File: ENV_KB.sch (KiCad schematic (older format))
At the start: 178 parts, among them J1 USB_B_Micro

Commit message: general housekeeping.
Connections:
- net USBVBUS: now reaches J1.1 (VBUS)
- net USBVBUS: now also RPI1.40 (VBUS)
- net USBDM: now reaches J1.2 (D-)
- net USBDM: now also RPI1.TP2 (USB_DM)
- net USBDP: now reaches J1.3 (D+)
- net USBDP: now also RPI1.TP3 (USB_DP)
- net USBGND: now reaches J1.5 (GND)
- net USBGND: now also RPI1.TP1 (GND_L)
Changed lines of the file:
@@
 Text GLabel 13750 10900 2    50   Input ~ 0
 col16
+Text GLabel 12800 8900 1    50   Input ~ 0
+USBGND
+Text GLabel 10800 9300 2    50   Input ~ 0
+USBGND
+Text GLabel 12950 8900 1    50   Input ~ 0
+USBDM
+Text GLabel 10500 9000 1    50   Input ~ 0
+USBDM
+Text GLabel 10400 9000 1    50   Input ~ 0
+USBDP
+Text GLabel 13100 8900 1    50   Input ~ 0
+USBDP
+Text GLabel 13650 9100 2    50   Input ~ 0
+USBVBUS
+Text GLabel 10200 9000 1    50   Input ~ 0
+USBVBUS
 $EndSCHEMATC

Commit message: This should be Ready.
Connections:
- net row0: now also RPI1.26 (GPIO20); no longer RPI1.34 (GPIO28_ADC2)
- net row2: now also RPI1.27 (GPIO21); no longer RPI1.32 (GPIO27_ADC1)
- net row3: now also RPI1.29 (GPIO22); no longer RPI1.31 (GPIO26_ADC0)
- net row4: now also RPI1.31 (GPIO26_ADC0); no longer RPI1.29 (GPIO22)
- net row5: now also RPI1.32 (GPIO27_ADC1); no longer RPI1.27 (GPIO21)
- net row6: now also RPI1.34 (GPIO28_ADC2); no longer RPI1.26 (GPIO20)
- net USBDM renamed USB2_N
- net USBDP renamed USB2_P
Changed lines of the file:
@@
 	0    -1   -1   0
 $EndComp
-Text GLabel 13750 10500 2    50   Input ~ 0
+Text GLabel 13750 9700 2    50   Input ~ 0
 row6
+Text GLabel 13750 9900 2    50   Input ~ 0
+row5
 Text GLabel 13750 10400 2    50   Input ~ 0
-row5
-Text GLabel 13750 9900 2    50   Input ~ 0
 row2
+Text GLabel 13750 10200 2    50   Input ~ 0
+row3
 Text GLabel 13750 10000 2    50   Input ~ 0
-row3
-Text GLabel 13750 10200 2    50   Input ~ 0
 row4
 Text GLabel 13750 10600 2    50   Input ~ 0
@@
 Text GLabel 13750 10700 2    50   Input ~ 0
 col15
-Text GLabel 13750 9700 2    50   Input ~ 0
+Text GLabel 13750 10500 2    50   Input ~ 0
 row0
 Wire Wire Line
@@
 USBGND
 Text GLabel 12950 8900 1    50   Input ~ 0
-USBDM
+USB2_N
 Text GLabel 10500 9000 1    50   Input ~ 0
-USBDM
+USB2_N
 Text GLabel 10400 9000 1    50   Input ~ 0
-USBDP
+USB2_P
 Text GLabel 13100 8900 1    50   Input ~ 0
-USBDP
+USB2_P
 Text GLabel 13650 9100 2    50   Input ~ 0
 USBVBUS

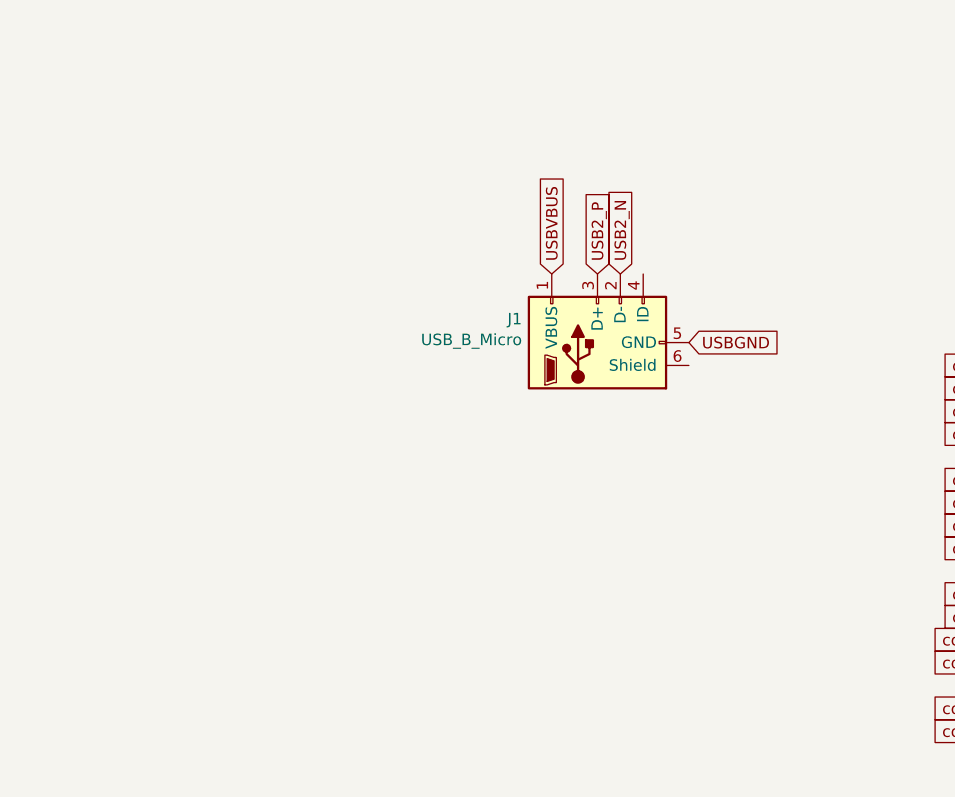
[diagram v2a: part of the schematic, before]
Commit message: replaced Micro B with Type C due to parts avaliability
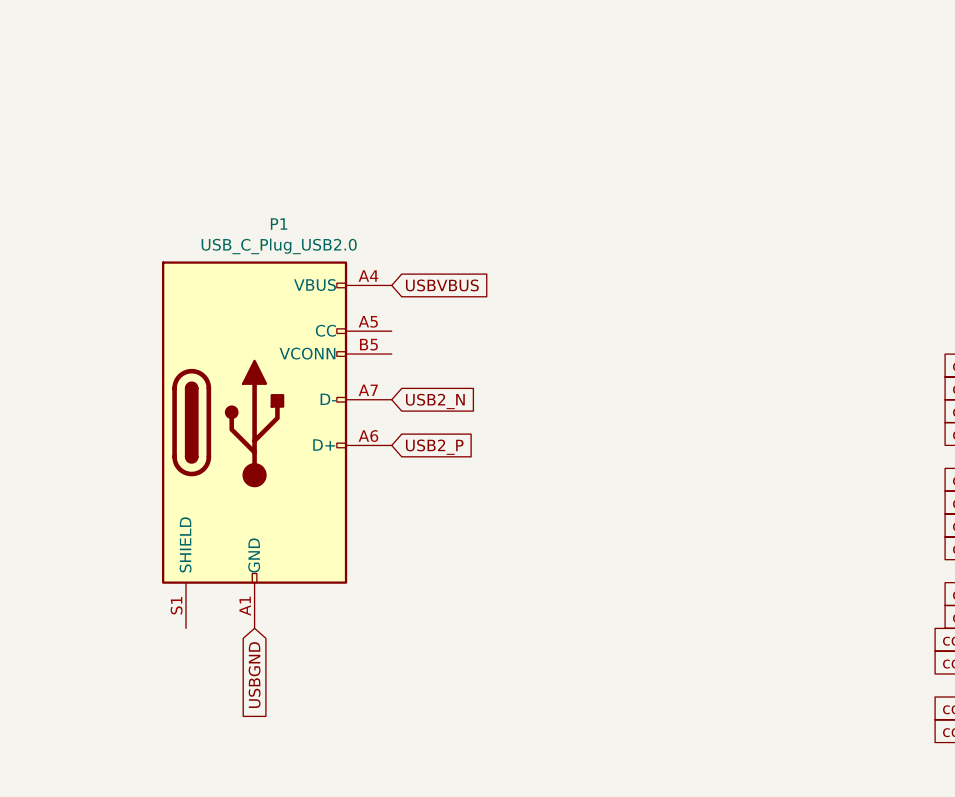
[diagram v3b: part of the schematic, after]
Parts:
- removed J1: USB_B_Micro, Connector_USB:USB_Micro-B_Wuerth_629105150521, symbol Connector:USB_B_Micro
- added P1: USB_C_Plug_USB2.0, Connector_USB:USB_C_Receptacle_HRO_TYPE-C-31-M-12, symbol Connector:USB_C_Plug_USB2.0
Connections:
- net USB2_N: now also P1.A7 (D-)
- net USB2_P: now also P1.A6 (D+)
- net USBGND: now also P1.A1 (GND), P1.A12 (GND), P1.B1 (GND), P1.B12 (GND)
- net USBVBUS: now also P1.A4 (VBUS), P1.A9 (VBUS), P1.B4 (VBUS), P1.B9 (VBUS)
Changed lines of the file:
@@
 	1    0    0    -1
-$EndComp
-$Comp
-L Connector:USB_B_Micro J1
-U 1 1 6031CA0E
-P 10400 9300
-F 0 "J1" V 10503 9630 50  0000 L CNN
-F 1 "USB_B_Micro" V 10412 9630 50  0000 L CNN
-F 2 "Connector_USB:USB_Micro-B_Wuerth_629105150521" H 10550 9250 50  0001 C CNN
-F 3 "~" H 10550 9250 50  0001 C CNN
-	1    10400 9300
-	0    -1   -1   0
 $EndComp
 Wire Wire Line
@@
 Text GLabel 12800 8900 1    50   Input ~ 0
 USBGND
-Text GLabel 10800 9300 2    50   Input ~ 0
-USBGND
 Text GLabel 12950 8900 1    50   Input ~ 0
 USB2_N
-Text GLabel 10500 9000 1    50   Input ~ 0
+Text GLabel 9500 9550 2    50   Input ~ 0
 USB2_N
-Text GLabel 10400 9000 1    50   Input ~ 0
+Text GLabel 9500 9750 2    50   Input ~ 0
 USB2_P
 Text GLabel 13100 8900 1    50   Input ~ 0
@@
 Text GLabel 13650 9100 2    50   Input ~ 0
 USBVBUS
-Text GLabel 10200 9000 1    50   Input ~ 0
+Text GLabel 8900 10550 3    50   Input ~ 0
+USBGND
+Text GLabel 9500 9050 2    50   Input ~ 0
 USBVBUS
+$Comp
+L Connector:USB_C_Plug_USB2.0 P1
+U 1 1 6035DC13
+P 8900 9650
+F 0 "P1" H 9007 10517 50  0000 C CNN
+F 1 "USB_C_Plug_USB2.0" H 9007 10426 50  0000 C CNN
+F 2 "Connector_USB:USB_C_Receptacle_HRO_TYPE-C-31-M-12" H 9050 9650 50  0001 C CNN
+F 3 "https://www.usb.org/sites/default/files/documents/usb_type-c.zip" H 9050 9650 50  0001 C CNN
+	1    8900 9650
+	1    0    0    -1
+$EndComp
 $EndSCHEMATC

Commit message: some random changes
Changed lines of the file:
@@
 	1350 3400 2350 3400
 Wire Wire Line
-	-50  2400 1450 2400
+	900  2400 2400 2400
 Wire Wire Line
 	1350 1400 3350 1400
@@
 $Comp
 L MX_Alps_Hybrid:MX-NoLED K_0
-U 1 1 00000001
+U 1 1 603522C8
 P 1400 1000
 F 0 "K_0" H 1400 1233 60  0000 C CNN
@@
 $Comp
 L MX_Alps_Hybrid:MX-NoLED K_1
-U 1 1 00000011
+U 1 1 603522CA
 P 3400 1000
 F 0 "K_1" H 3400 1233 60  0000 C CNN
@@
 $Comp
 L MX_Alps_Hybrid:MX-NoLED K_3
-U 1 1 00000031
+U 1 1 603522CE
 P 5400 1000
 F 0 "K_3" H 5400 1233 60  0000 C CNN
@@
 $Comp
 L MX_Alps_Hybrid:MX-NoLED K_4
-U 1 1 00000041
+U 1 1 603522D0
 P 6400 1000
 F 0 "K_4" H 6400 1233 60  0000 C CNN
@@
 $Comp
 L MX_Alps_Hybrid:MX-NoLED K_5
-U 1 1 00000051
+U 1 1 603522D2
 P 8400 1000
 F 0 "K_5" H 8400 1233 60  0000 C CNN
@@
 $Comp
 L MX_Alps_Hybrid:MX-NoLED K_7
-U 1 1 00000071
+U 1 1 603522D6
 P 10400 1000
 F 0 "K_7" H 10400 1233 60  0000 C CNN
@@
 $Comp
 L Device:D_Small D7
-U 1 1 00000070
+U 1 1 603522D5
 P 10350 1300
 F 0 "D7" V 10420 1200 50  0000 R CNN
@@
 $Comp
 L Device:D_Small D8
-U 1 1 00000080
+U 1 1 603522D7
 P 11350 1300
 F 0 "D8" V 11420 1200 50  0000 R CNN
@@
 $Comp
 L MX_Alps_Hybrid:MX-NoLED K_9
-U 1 1 00000091
+U 1 1 603522DA
 P 12400 1000
 F 0 "K_9" H 12400 1233 60  0000 C CNN
@@
 $Comp
 L Device:D_Small D9
-U 1 1 00000090
+U 1 1 603522D9
 P 12350 1300
 F 0 "D9" V 12420 1200 50  0000 R CNN
@@
 $Comp
 L MX_Alps_Hybrid:MX-NoLED K_10
-U 1 1 00000101
+U 1 1 603522DC
 P 13400 1000
 F 0 "K_10" H 13400 1233 60  0000 C CNN
@@
 $Comp
 L Device:D_Small D6
-U 1 1 00000060
+U 1 1 603522D3
 P 9350 1300
 F 0 "D6" V 9420 1200 50  0000 R CNN
@@
 $Comp
 L Device:D_Small D5
-U 1 1 00000050
+U 1 1 603522D1
 P 8350 1300
 F 0 "D5" V 8420 1200 50  0000 R CNN
@@
 $Comp
 L Device:D_Small D4
-U 1 1 00000040
+U 1 1 603522CF
 P 6350 1300
 F 0 "D4" V 6420 1200 50  0000 R CNN
@@
 $Comp
 L Device:D_Small D3
-U 1 1 00000030
+U 1 1 603522CD
 P 5350 1300
 F 0 "D3" V 5420 1200 50  0000 R CNN
@@
 $Comp
 L Device:D_Small D2
-U 1 1 00000020
+U 1 1 603522CB
 P 4350 1300
 F 0 "D2" V 4420 1200 50  0000 R CNN

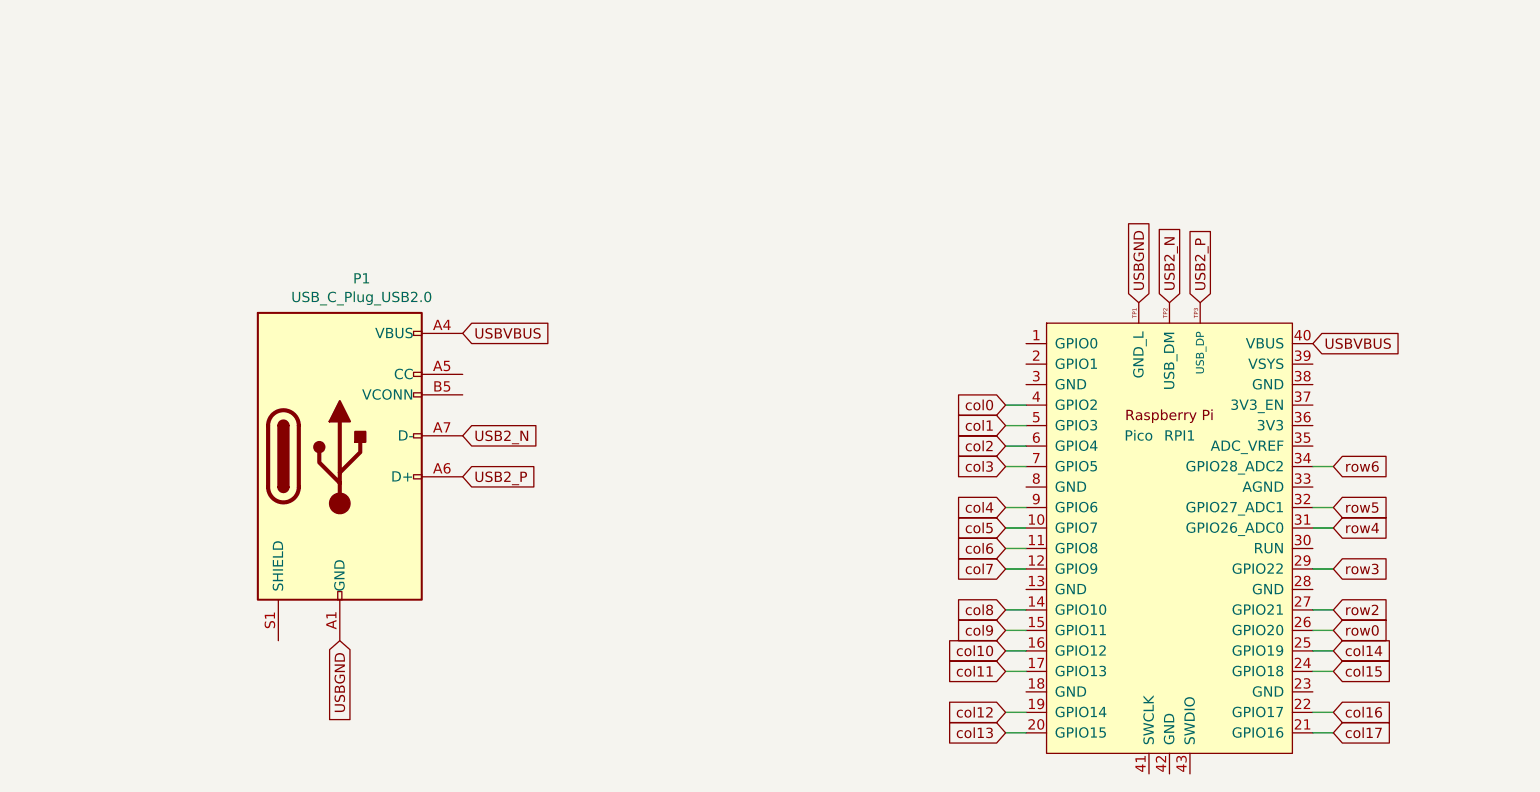
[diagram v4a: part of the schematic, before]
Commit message: Adjusted things + typeC CC pins
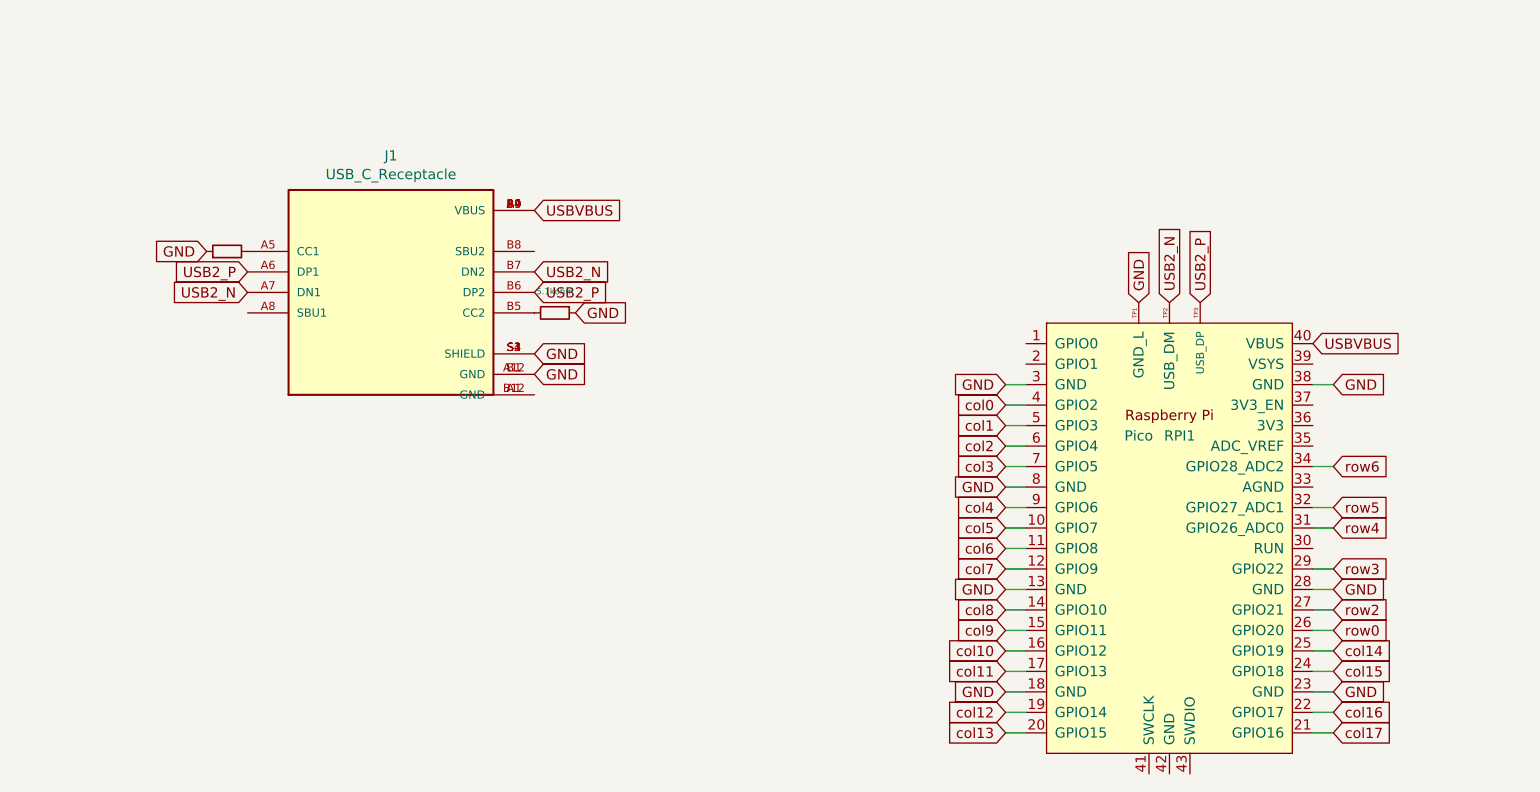
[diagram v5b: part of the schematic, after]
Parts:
- removed P1: USB_C_Plug_USB2.0, Connector_USB:USB_C_Receptacle_HRO_TYPE-C-31-M-12, symbol Connector:USB_C_Plug_USB2.0
- added J1: USB_C_Receptacle, Type-C-Bits:HRO_TYPE-C-31-M-12, symbol Type-C-Lib:TYPE-C-31-M-12
- added RESISTOR1, RESISTOR2: 5.1kohm, Resistor_SMD:R_0402_1005Metric, symbol Device:R_Small
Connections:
- net USBGND is gone; now on net GND: RPI1.TP1 (GND_L)
- net USB2_N: now also J1.A7 (DN1), J1.B7 (DN2)
- net USB2_P: now also J1.A6 (DP1), J1.B6 (DP2)
- net USBVBUS: now also J1.A4 (VBUS), J1.A9 (VBUS), J1.B4 (VBUS), J1.B9 (VBUS)
- net GND: now reaches RPI1.13 (GND)
- net GND: now also RPI1.18 (GND), RPI1.23 (GND), RPI1.28 (GND), RPI1.3 (GND), RPI1.38 (GND), RPI1.8 (GND), J1.A12 (GND), J1.B1 (GND), J1.S1 (SHIELD), J1.S2 (SHIELD), J1.S3 (SHIELD), J1.S4 (SHIELD), RESISTOR1.1, RESISTOR2.1
- new net: J1.B5 (CC2), RESISTOR1.2
- new net: J1.A5 (CC1), RESISTOR2.2
- new net: J1.A1 (GND), J1.B12 (GND)
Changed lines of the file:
@@
 col16
 Text GLabel 12800 8900 1    50   Input ~ 0
-USBGND
+GND
 Text GLabel 12950 8900 1    50   Input ~ 0
 USB2_N
-Text GLabel 9500 9550 2    50   Input ~ 0
+Text GLabel 8450 8850 0    50   Input ~ 0
 USB2_N
-Text GLabel 9500 9750 2    50   Input ~ 0
+Text GLabel 9850 8850 2    50   Input ~ 0
 USB2_P
 Text GLabel 13100 8900 1    50   Input ~ 0
@@
 Text GLabel 13650 9100 2    50   Input ~ 0
 USBVBUS
-Text GLabel 8900 10550 3    50   Input ~ 0
-USBGND
-Text GLabel 9500 9050 2    50   Input ~ 0
+Text GLabel 9850 8450 2    50   Input ~ 0
 USBVBUS
+Text GLabel 10050 8950 2    50   Input ~ 0
+GND
+Text GLabel 12150 9300 0    50   Input ~ 0
+GND
+Text GLabel 12150 9800 0    50   Input ~ 0
+GND
+Text GLabel 12150 10300 0    50   Input ~ 0
+GND
+Text GLabel 12150 10800 0    50   Input ~ 0
+GND
+Text GLabel 13750 10800 2    50   Input ~ 0
+GND
+Text GLabel 13750 10300 2    50   Input ~ 0
+GND
+Text GLabel 13750 9300 2    50   Input ~ 0
+GND
+Wire Wire Line
+	13650 9300 13750 9300
+Wire Wire Line
+	12250 9300 12150 9300
+Wire Wire Line
+	12150 9800 12250 9800
+Wire Wire Line
+	12150 10300 12250 10300
+Wire Wire Line
+	12150 10800 12250 10800
+Wire Wire Line
+	13650 10800 13750 10800
+Wire Wire Line
+	13650 10300 13750 10300
 $Comp
-L Connector:USB_C_Plug_USB2.0 P1
-U 1 1 6035DC13
-P 8900 9650
-F 0 "P1" H 9007 10517 50  0000 C CNN
-F 1 "USB_C_Plug_USB2.0" H 9007 10426 50  0000 C CNN
-F 2 "Connector_USB:USB_C_Receptacle_HRO_TYPE-C-31-M-12" H 9050 9650 50  0001 C CNN
-F 3 "https://www.usb.org/sites/default/files/documents/usb_type-c.zip" H 9050 9650 50  0001 C CNN
-	1    8900 9650
+L Device:R_Small RESISTOR1
+U 1 1 606333E5
+P 9950 8950
+F 0 "RESISTOR1" V 9754 8950 39  0001 C CNN
+F 1 "5.1kohm" V 9845 8950 30  0000 C CNN
+F 2 "Resistor_SMD:R_0402_1005Metric" H 9950 8950 50  0001 C CNN
+F 3 "~" H 9950 8950 50  0001 C CNN
+	1    9950 8950
+	0    1    1    0
+$EndComp
+$Comp
+L Device:R_Small RESISTOR2
+U 1 1 6066AF89
+P 8350 8650
+F 0 "RESISTOR2" V 8154 8650 39  0001 C CNN
+F 1 "5.1kohm" V 8245 8650 50  0001 C CNN
+F 2 "Resistor_SMD:R_0402_1005Metric" H 8350 8650 50  0001 C CNN
+F 3 "~" H 8350 8650 50  0001 C CNN
+	1    8350 8650
+	0    -1   -1   0
+$EndComp
+Text GLabel 8250 8650 0    50   Input ~ 0
+GND
+Text GLabel 9850 9150 2    50   Input ~ 0
+GND
+Text GLabel 9850 9250 2    50   Input ~ 0
+GND
+$Comp
+L Type-C-Lib:TYPE-C-31-M-12 J1
+U 1 1 607F5ECC
+P 9150 8850
+F 0 "J1" H 9150 9517 50  0000 C CNN
+F 1 "USB_C_Receptacle" H 9150 9426 50  0000 C CNN
+F 2 "Type-C-Bits:HRO_TYPE-C-31-M-12" H 9300 8850 50  0001 C CNN
+F 3 "https://www.usb.org/sites/default/files/documents/usb_type-c.zip" H 9300 8850 50  0001 C CNN
+	1    9150 8850
 	1    0    0    -1
 $EndComp
+Text GLabel 9850 8750 2    50   Input ~ 0
+USB2_N
+Text GLabel 8450 8750 0    50   Input ~ 0
+USB2_P
 $EndSCHEMATC

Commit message: some adjustments
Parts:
- J1: value USB_C_Receptacle -> TYPE-C-31-M-12; footprint Type-C-Bits:HRO_TYPE-C-31-M-12 -> HRO_TYPE-C-31-M-12; MANUFACTURER (none) -> HRO Electronics; MAXIMUM_PACKAGE_HEIGHT (none) -> 3.31mm; PARTREV (none) -> A; STANDARD (none) -> Manufacturer Recommendations
- RPI1: footprint MCU_RaspberryPi_and_Boards.pretty:RPi_Pico_SMD_TH -> EM_Extras:RPi_Pico_SMD_TH
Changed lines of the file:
@@
 F 0 "RPI1" H 13000 10550 50  0000 C CNN
 F 1 "Pico" H 12800 10550 50  0000 C CNN
-F 2 "MCU_RaspberryPi_and_Boards.pretty:RPi_Pico_SMD_TH" V 12950 10050 50  0001 C CNN
+F 2 "EM_Extras:RPi_Pico_SMD_TH" V 12950 10050 50  0001 C CNN
 F 3 "" H 12950 10050 50  0001 C CNN
 	1    12950 10050
@@
 P 9950 8950
 F 0 "RESISTOR1" V 9754 8950 39  0001 C CNN
-F 1 "5.1kohm" V 9845 8950 30  0000 C CNN
+F 1 "5.1kohm" V 10050 8950 30  0000 C CNN
 F 2 "Resistor_SMD:R_0402_1005Metric" H 9950 8950 50  0001 C CNN
 F 3 "~" H 9950 8950 50  0001 C CNN
@@
 P 9150 8850
 F 0 "J1" H 9150 9517 50  0000 C CNN
-F 1 "USB_C_Receptacle" H 9150 9426 50  0000 C CNN
-F 2 "Type-C-Bits:HRO_TYPE-C-31-M-12" H 9300 8850 50  0001 C CNN
-F 3 "https://www.usb.org/sites/default/files/documents/usb_type-c.zip" H 9300 8850 50  0001 C CNN
+F 1 "TYPE-C-31-M-12" H 9150 9426 50  0000 C CNN
+F 2 "HRO_TYPE-C-31-M-12" H 9150 8250 50  0000 C CNN
+F 3 "~" H 9300 8850 50  0001 C CNN
+F 4 "HRO Electronics" H 9150 8850 50  0001 C CNN "MANUFACTURER"
+F 5 "3.31mm" H 9150 8850 50  0001 C CNN "MAXIMUM_PACKAGE_HEIGHT"
+F 6 "A" H 9150 8850 50  0001 C CNN "PARTREV"
+F 7 "Manufacturer Recommendations" H 9150 8850 50  0001 C CNN "STANDARD"
 	1    9150 8850
 	1    0    0    -1
